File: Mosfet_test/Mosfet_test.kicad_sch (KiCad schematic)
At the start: 6 parts, among them Q1 NMOS

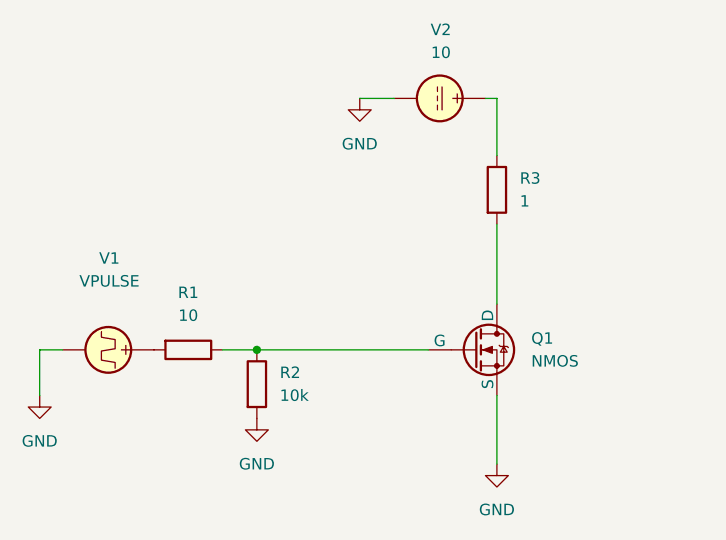
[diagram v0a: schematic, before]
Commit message: EDM_Powersupply in LTSpice :)
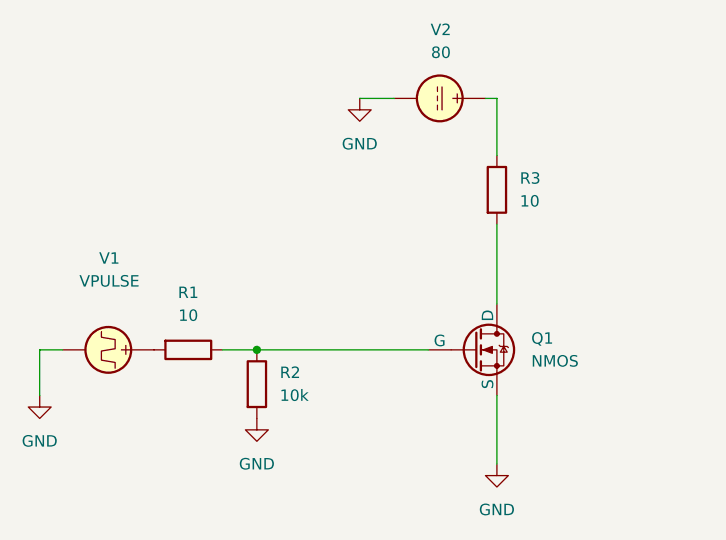
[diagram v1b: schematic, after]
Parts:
- R3: value 1 -> 10
- V2: value 10 -> 80
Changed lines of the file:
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@@
 		)
 		(instances
-			(project "Main_topology"
+			(project "Mosfet_test"
 				(path "/d48048dc-112f-48cd-b9ca-e7317887f716"
 					(reference "Q1")
@@
 		)
 		(instances
-			(project "Main_topology"
+			(project "Mosfet_test"
 				(path "/d48048dc-112f-48cd-b9ca-e7317887f716"
 					(reference "#PWR03")
@@
 		)
 		(instances
-			(project "Main_topology"
+			(project "Mosfet_test"
 				(path "/d48048dc-112f-48cd-b9ca-e7317887f716"
 					(reference "#PWR04")
@@
 			)
 		)
-		(property "Value" "1"
+		(property "Value" "10"
 			(at 168.91 64.7699 0)
 			(effects
@@
 		)
 		(instances
-			(project "Main_topology"
+			(project "Mosfet_test"
 				(path "/d48048dc-112f-48cd-b9ca-e7317887f716"
 					(reference "R3")
@@
 		)
 		(instances
-			(project "Main_topology"
+			(project "Mosfet_test"
 				(path "/d48048dc-112f-48cd-b9ca-e7317887f716"
 					(reference "V1")
@@
 		)
 		(instances
-			(project "Main_topology"
+			(project "Mosfet_test"
 				(path "/d48048dc-112f-48cd-b9ca-e7317887f716"
 					(reference "#PWR01")
@@
 		)
 		(instances
-			(project "Main_topology"
+			(project "Mosfet_test"
 				(path "/d48048dc-112f-48cd-b9ca-e7317887f716"
 					(reference "R2")
@@
 		)
 		(instances
-			(project "Main_topology"
+			(project "Mosfet_test"
 				(path "/d48048dc-112f-48cd-b9ca-e7317887f716"
 					(reference "R1")
@@
 		)
 		(instances
-			(project "Main_topology"
+			(project "Mosfet_test"
 				(path "/d48048dc-112f-48cd-b9ca-e7317887f716"
 					(reference "#PWR02")
@@
 			)
 		)
-		(property "Value" "10"
+		(property "Value" "80"
 			(at 160.1498 48.26 90)
 			(effects
@@
 		)
 		(instances
-			(project "Main_topology"
+			(project "Mosfet_test"
 				(path "/d48048dc-112f-48cd-b9ca-e7317887f716"
 					(reference "V2")

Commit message: Investigated oscillations from voltage across R_currentlimiting after t_off
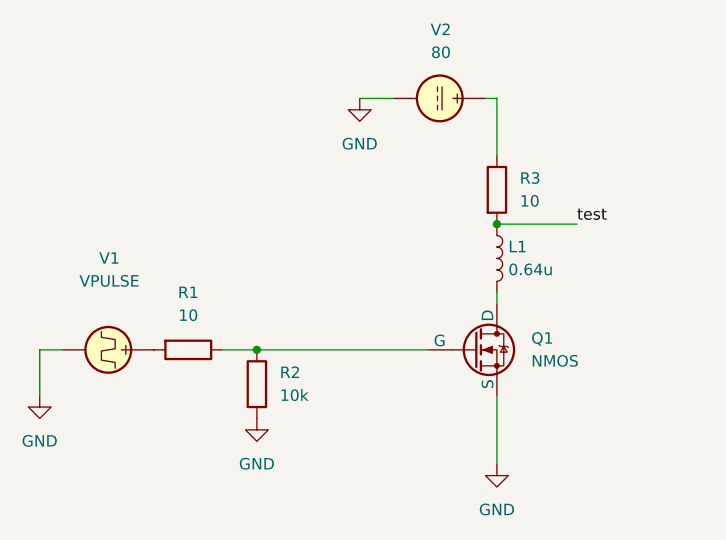
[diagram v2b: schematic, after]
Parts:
- added L1: 0.64u, symbol Device:L
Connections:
- net at Q1.1 (D): now also L1.2; no longer R3.2
- new net test: L1.1, R3.2
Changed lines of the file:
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@@
 	(paper "A4")
+	(junction
+		(at 166.37 67.31)
+		(diameter 0)
+		(color 0 0 0 0)
+	)
 	(junction
 		(at 139.7 81.28)
@@
 	(wire
 		(pts
-			(xy 166.37 67.31) (xy 166.37 76.2)
-		)
-		(stroke
-			(width 0)
-			(type default)
-		)
-	)
-	(wire
-		(pts
 			(xy 118.11 81.28) (xy 115.57 81.28)
 		)
@@
 	(wire
 		(pts
+			(xy 166.37 67.31) (xy 175.26 67.31)
+		)
+		(stroke
+			(width 0)
+			(type default)
+		)
+	)
+	(wire
+		(pts
 			(xy 166.37 59.69) (xy 166.37 53.34)
 		)
@@
 	(wire
 		(pts
+			(xy 166.37 74.93) (xy 166.37 76.2)
+		)
+		(stroke
+			(width 0)
+			(type default)
+		)
+	)
+	(wire
+		(pts
 			(xy 165.1 53.34) (xy 166.37 53.34)
 		)
@@
 			(width 0)
 			(type default)
+		)
+	)
+	(label "test"
+		(at 175.26 67.31 0)
+		(fields_autoplaced yes)
+		(effects
+			(font
+				(size 1.27 1.27)
+			)
+			(justify left bottom)
 		)
 	)
@@
 		)
 		(property "Sim.Device" "NMOS"
-			(at 163.83 98.425 0)
+			(at 163.83 81.28 0)
+			(effects
+				(font
+					(size 1.27 1.27)
+				)
+				(hide yes)
+			)
+		)
+		(property "Sim.Pins" "1=D 2=G 3=S"
+			(at 163.83 81.28 0)
 			(effects
 				(font
@@
 		)
 		(property "Sim.Type" "VDMOS"
-			(at 163.83 100.33 0)
-			(effects
-				(font
-					(size 1.27 1.27)
-				)
-				(hide yes)
-			)
-		)
-		(property "Sim.Pins" "1=D 2=G 3=S"
-			(at 163.83 96.52 0)
+			(at 163.83 81.28 0)
 			(effects
 				(font
@@
 					(unit 1)
 				)
+			)
+		)
+	)
+	(symbol
+		(lib_id "Device:L")
+		(at 166.37 71.12 0)
+		(unit 1)
+		(exclude_from_sim no)
+		(in_bom yes)
+		(on_board yes)
+		(dnp no)
+		(fields_autoplaced yes)
+		(property "Reference" "L1"
+			(at 167.64 69.8499 0)
+			(effects
+				(font
+					(size 1.27 1.27)
+				)
+				(justify left)
+			)
+		)
+		(property "Value" "0.64u"
+			(at 167.64 72.3899 0)
+			(effects
+				(font
+					(size 1.27 1.27)
+				)
+				(justify left)
+			)
+		)
+		(property "Footprint" ""
+			(at 166.37 71.12 0)
+			(effects
+				(font
+					(size 1.27 1.27)
+				)
+				(hide yes)
+			)
+		)
+		(property "Datasheet" "~"
+			(at 166.37 71.12 0)
+			(effects
+				(font
+					(size 1.27 1.27)
+				)
+				(hide yes)
+			)
+		)
+		(property "Description" "Inductor"
+			(at 166.37 71.12 0)
+			(effects
+				(font
+					(size 1.27 1.27)
+				)
+				(hide yes)
+			)
+		)
+		(pin "2"
+		)
+		(pin "1"
+		)
+		(instances
+			(project "Mosfet_test"
+				(path "/d48048dc-112f-48cd-b9ca-e7317887f716"
+					(reference "L1")
+					(unit 1)
+				)

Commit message: Kicad oscillatie fix met diode
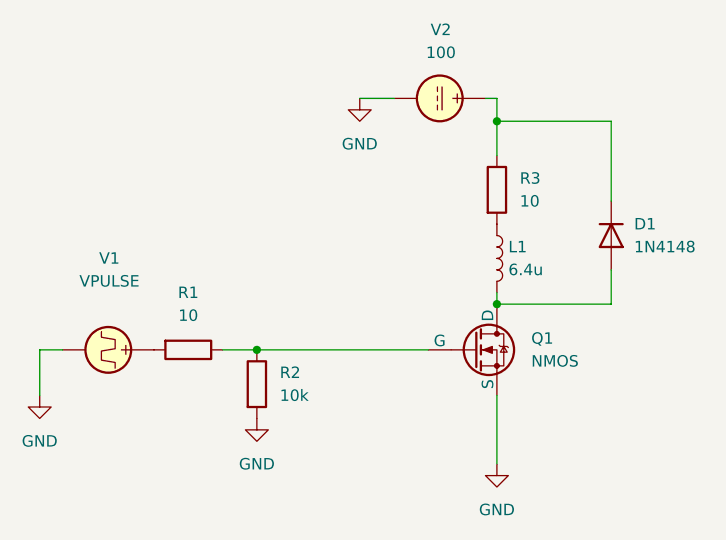
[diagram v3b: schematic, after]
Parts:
- added D1: 1N4148, Diode_THT:D_DO-35_SOD27_P7.62mm_Horizontal, symbol Diode:1N4148
- L1: value 0.64u -> 6.4u
- V2: value 80 -> 100
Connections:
- net at L1.2, Q1.1 (D): now also D1.2 (A)
- net at R3.1, V2.1: now also D1.1 (K)
- net test: no longer names the net of L1.1, R3.2
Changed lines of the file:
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@@
 	(paper "A4")
 	(junction
-		(at 166.37 67.31)
+		(at 166.37 76.2)
+		(diameter 0)
+		(color 0 0 0 0)
+	)
+	(junction
+		(at 166.37 55.88)
 		(diameter 0)
 		(color 0 0 0 0)
@@
 	(wire
 		(pts
+			(xy 166.37 76.2) (xy 179.07 76.2)
+		)
+		(stroke
+			(width 0)
+			(type default)
+		)
+	)
+	(wire
+		(pts
 			(xy 118.11 81.28) (xy 115.57 81.28)
 		)
@@
 	(wire
 		(pts
-			(xy 166.37 67.31) (xy 175.26 67.31)
-		)
-		(stroke
-			(width 0)
-			(type default)
-		)
-	)
-	(wire
-		(pts
-			(xy 166.37 59.69) (xy 166.37 53.34)
+			(xy 166.37 53.34) (xy 166.37 55.88)
+		)
+		(stroke
+			(width 0)
+			(type default)
+		)
+	)
+	(wire
+		(pts
+			(xy 179.07 72.39) (xy 179.07 76.2)
 		)
 		(stroke
@@
 	(wire
 		(pts
+			(xy 166.37 55.88) (xy 179.07 55.88)
+		)
+		(stroke
+			(width 0)
+			(type default)
+		)
+	)
+	(wire
+		(pts
+			(xy 166.37 55.88) (xy 166.37 59.69)
+		)
+		(stroke
+			(width 0)
+			(type default)
+		)
+	)
+	(wire
+		(pts
 			(xy 139.7 81.28) (xy 158.75 81.28)
 		)
@@
 		)
 	)
-	(label "test"
-		(at 175.26 67.31 0)
-		(fields_autoplaced yes)
-		(effects
-			(font
-				(size 1.27 1.27)
-			)
-			(justify left bottom)
+	(wire
+		(pts
+			(xy 179.07 55.88) (xy 179.07 64.77)
+		)
+		(stroke
+			(width 0)
+			(type default)
 		)
 	)
@@
 			)
 		)
-		(property "Value" "0.64u"
+		(property "Value" "6.4u"
 			(at 167.64 72.3899 0)
 			(effects
@@
 			)
 		)
-		(property "Sim.Params" "y1=0 y2=5 td=0 tr=2n tf=2n  tw=500n per=1000n"
+		(property "Sim.Params" "y1=0 y2=5 td=0 tr=2n tf=2n  tw=2u per=20u"
 			(at 123.3198 76.2 90)
 			(effects
@@
 	)
 	(symbol
+		(lib_id "Diode:1N4148")
+		(at 179.07 68.58 270)
+		(unit 1)
+		(exclude_from_sim no)
+		(in_bom yes)
+		(on_board yes)
+		(dnp no)
+		(fields_autoplaced yes)
+		(property "Reference" "D1"
+			(at 181.61 67.3099 90)
+			(effects
+				(font
+					(size 1.27 1.27)
+				)
+				(justify left)
+			)
+		)
+		(property "Value" "1N4148"
+			(at 181.61 69.8499 90)
+			(effects
+				(font
+					(size 1.27 1.27)
+				)
+				(justify left)
+			)
+		)
+		(property "Footprint" "Diode_THT:D_DO-35_SOD27_P7.62mm_Horizontal"
+			(at 179.07 68.58 0)
+			(effects
+				(font
+					(size 1.27 1.27)
+				)
+				(hide yes)
+			)
+		)
+		(property "Datasheet" "https://assets.nexperia.com/documents/data-sheet/1N4148_1N4448.pdf"
+			(at 179.07 68.58 0)
+			(effects
+				(font
+					(size 1.27 1.27)
+				)
+				(hide yes)
+			)
+		)
+		(property "Description" "100V 0.15A standard switching diode, DO-35"
+			(at 179.07 68.58 0)
+			(effects
+				(font
+					(size 1.27 1.27)
+				)
+				(hide yes)
+			)
+		)
+		(property "Sim.Device" "D"
+			(at 179.07 68.58 0)
+			(effects
+				(font
+					(size 1.27 1.27)
+				)
+				(hide yes)
+			)
+		)
+		(property "Sim.Pins" "1=K 2=A"
+			(at 179.07 68.58 0)
+			(effects
+				(font
+					(size 1.27 1.27)
+				)
+				(hide yes)
+			)
+		)
+		(pin "1"
+		)
+		(pin "2"
+		)
+		(instances
+			(project "Mosfet_test"
+				(path "/d48048dc-112f-48cd-b9ca-e7317887f716"
+					(reference "D1")
+					(unit 1)
+				)
+			)
+		)
+	)
+	(symbol
 		(lib_id "Simulation_SPICE:VDC")
 		(at 160.02 53.34 270)
@@
 			)
 		)
-		(property "Value" "80"
+		(property "Value" "100"
 			(at 160.1498 48.26 90)
 			(effects
